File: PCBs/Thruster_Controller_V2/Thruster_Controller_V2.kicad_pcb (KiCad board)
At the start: 4 copper layers, 35.5 x 37 mm, 106 parts, among them J1 PHASE_A, J2 PHASE_B, J3 PHASE_C, J4 Conn_01x01, J5 Pogo Conn, J6 Conn_01x01, J7 Conn_01x01, J8 Conn_01x01, Q1 SIZF906DT, Q2 SIZF906DT, Q3 SIZF906DT, U1 NCP718AMT330, U2 TMS320F280041C, U3 DRV8320S, U8 MCP2562, Y1 20 MHz

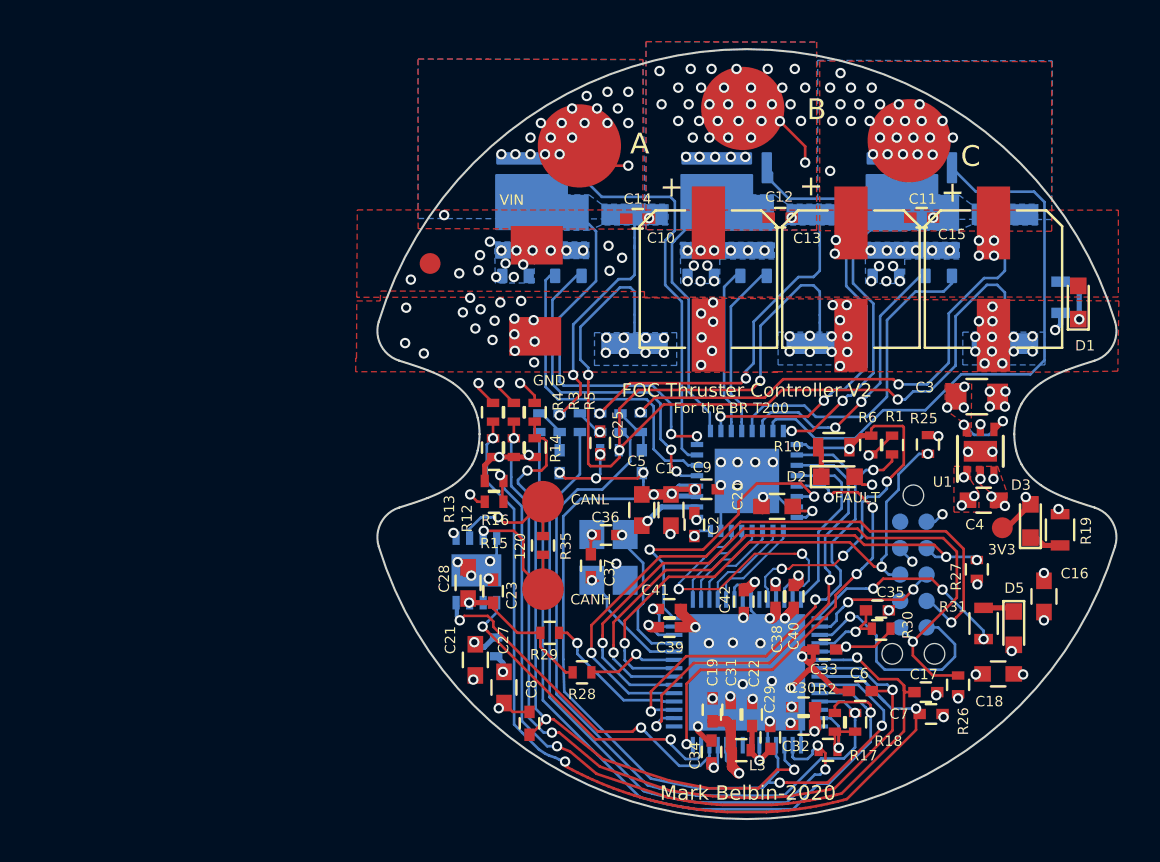
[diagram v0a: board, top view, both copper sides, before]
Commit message: VDD fix
- Fixed VDD error, disconnected it from 3V3 rail.
- Will add any more updates to V2.1 after V2 testing
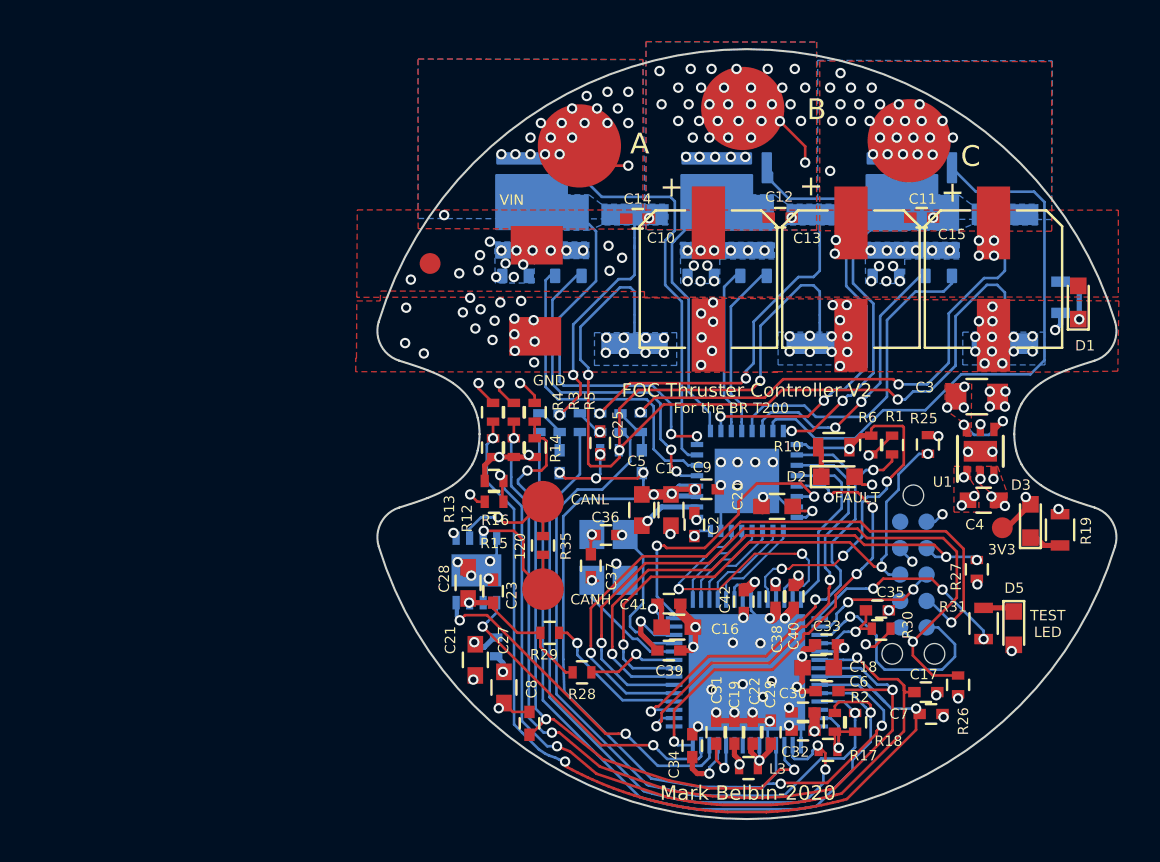
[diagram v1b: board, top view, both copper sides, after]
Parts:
- R19: value 330 -> 180
- moved C16 17.7 mm to (96.7, 107.5), turned to 0 degrees
- moved C18 8.66 mm to (103.4, 109.5), turned to 180 degrees
- moved C6 1.60 mm to (103.8, 110.6)
- moved C19 1.50 mm to (99.4, 112.6)
- moved C39 1.13 mm to (96.2, 108.7)
- moved C31 1.10 mm to (98.5, 112.6)
- moved C34 0.97 mm to (97.4, 113.2)
- moved L3 0.93 mm to (100.1, 114.3)
- moved C22 0.85 mm to (100.3, 112.6)
- moved C32 0.28 mm to (102.7, 112.5)
- moved C33 0.26 mm to (103.8, 108.3)
- moved C29 0.25 mm to (101.2, 112.6)
- moved C41 0.25 mm to (96.2, 106.4)
- moved C30 0.25 mm to (102.7, 111.6)
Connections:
- C16 pad 1: +3V3 -> Net-(C16-Pad1)
- C18 pad 1: +3V3 -> Net-(C18-Pad1)
- C31 pad 1: +3V3 -> Net-(C31-Pad1)
- C33 pad 1: +3V3 -> Net-(C18-Pad1)
- C38 pad 1: +3V3 -> Net-(C38-Pad1)
- C41 pad 1: +3V3 -> Net-(C16-Pad1)
- U2 pad 24: +3V3 -> Net-(C31-Pad1)
- U2 pad 41: +3V3 -> Net-(C16-Pad1)
- U2 pad 5: +3V3 -> Net-(C18-Pad1)
- U2 pad 53: +3V3 -> Net-(C38-Pad1)
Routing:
- net +3V3: track 31.6 -> 18.6 mm, vias 20 -> 16
- net +3.3VA: track 8.61 -> 11.9 mm
- net Net-(C16-Pad1): track 0.00 -> 2.82 mm, vias 0 -> 1
- net Net-(C18-Pad1): track 0.00 -> 2.52 mm, vias 0 -> 1
- net Net-(C31-Pad1): track 0.00 -> 2.46 mm, vias 0 -> 1
- net /Powertrain/VSEN_B: track 41.4 -> 43.1 mm
- net Net-(C38-Pad1): track 0.00 -> 0.92 mm, vias 0 -> 1
- net GND: track 42.5 -> 41.6 mm
- net Net-(C22-Pad1): track 3.39 -> 2.69 mm
- net /TDO: track 34.4 -> 35.0 mm
- net /TCK: track 32.1 -> 32.7 mm
- net /TMS: track 25.8 -> 26.4 mm
- net /TDI: track 26.5 -> 27.0 mm
- net /Powertrain/SPI_CS: track 21.9 -> 22.4 mm
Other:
- board text added: "TEST LED"

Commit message: Layout Changes
- Flipping 3V3 regulator to the bottom of the board for better thermal performance.
- Likewise placing 5V regulator on the bottom. This will require mech changes.
- Need to compress things to the right more
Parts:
- added C43: 1uF, Capacitors_SMD:C_0805, F.Cu at (67.9, 102.6)
- added C44: 1uF, Capacitors_SMD:C_0603, F.Cu at (71.9, 105.2)
- added D4: GREEN, LEDs:LED_0603, F.Cu at (72.1, 102.3)
- added R34: 220, Resistors_SMD:R_0603, F.Cu at (75.9, 102.4)
- added TP2: TestPoint, Thruster_Controller:TestPoint_Pad_D1.0mm, F.Cu at (74.8, 104.6)
- added U4: NCP718BMT500, Housings_DFN_QFN:DFN-6-1EP_2x2mm_Pitch0.65mm, B.Cu at (86.8, 105.4)
- R19: value 180 -> 100
- U8: value MCP2562 -> ATA6561; moved to F.Cu
- moved J4 7.06 mm to (91.0, 108.5)
- moved R29 5.38 mm to (95.1, 110.6), turned to 180 degrees
- moved R35 3.87 mm to (92.0, 107.0), turned to 90 degrees
- moved R28 3.02 mm to (95.1, 109.7), turned to 180 degrees
- moved C28 2.76 mm to (89.4, 105.4)
- moved C23 2.31 mm to (89.6, 107.2), turned to 0 degrees
- moved J6 0.76 mm to (91.0, 105.6)
- moved U8 0.68 mm to (86.8, 105.5)
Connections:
- C23 pad 1: +3V3 -> +5V
- C28 pad 1: +3V3 -> +5V
- U8 pad 3: +3V3 -> +5V
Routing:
- net +3V3: track 18.6 -> 11.4 mm, vias 16 -> 14
- net /CANH: track 6.84 -> 0.00 mm, vias 1 -> 0
- net /CANL: track 6.58 -> 0.00 mm, vias 1 -> 0
- net /TI_MCU/GPIO24: track 7.23 -> 2.76 mm
- net /RXCAN: track 17.2 -> 14.4 mm, vias 2 -> 1
- net /TI_MCU/GPIO32: track 4.37 -> 2.81 mm
- net GND: track 41.6 -> 40.6 mm
- net /Powertrain/PGA_GND: track 44.3 -> 43.5 mm
- net /TXCAN: track 15.2 -> 15.7 mm, vias 2 -> 1
- net +5V: track 0.00 -> 0.18 mm, vias 0 -> 1
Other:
- board text added: "FOC Thruster Controller V2.1"
- board text removed: "FOC Thruster Controller V2"

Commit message: Routing and Layout
- Finished layout
- Finished routing
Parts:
- L1: moved to F.Cu
- U1, U8: moved to B.Cu
- moved TP2 16.7 mm to (91.0, 108.5)
- moved C43 16.7 mm to (84.5, 103.1), turned to 180 degrees
- moved D4 13.6 mm to (85.2, 106.1)
- moved C44 12.7 mm to (84.5, 104.7), turned to 180 degrees
- moved R34 11.6 mm to (86.0, 108.1), turned to 270 degrees
- moved J6 4.00 mm to (91.0, 101.6)
- moved R35 3.95 mm to (90.0, 103.7)
- moved J4 2.92 mm to (91.0, 105.6)
- moved U4 2.92 mm to (84.5, 103.7)
- moved C23 2.68 mm to (88.5, 104.8), turned to 90 degrees
- moved C4 2.40 mm to (111.0, 99.0), turned to 180 degrees
- moved C28 2.05 mm to (87.3, 105.0)
- moved U8 1.46 mm to (87.7, 104.2)
- moved U1 1.24 mm to (111.0, 97.8)
- moved C36 1.14 mm to (94.2, 103.7)
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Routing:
- net +3V3: track 11.4 -> 25.9 mm, vias 14 -> 16
- net GND: track 40.6 -> 49.5 mm, vias 111 -> 112
- net /CANL: track 0.00 -> 6.25 mm, vias 0 -> 1
- net /CANH: track 0.00 -> 5.19 mm, vias 0 -> 1
- net +5V: track 0.18 -> 5.06 mm, vias 1 -> 4
- net /RXCAN: track 14.4 -> 17.7 mm, vias 1 -> 2
- net Net-(D4-Pad1): track 0.00 -> 2.55 mm
- net +BATT: track 11.0 -> 12.9 mm
- net /TI_MCU/GPIO24: track 2.76 -> 4.14 mm
- net /Powertrain/EN_GATE: track 14.2 -> 13.1 mm
- net /Powertrain/VSEN_PVDD: track 41.7 -> 42.6 mm
- net /TXCAN: track 15.7 -> 14.9 mm, vias 1 -> 2
- net /Powertrain/ISEN_C: track 35.6 -> 34.9 mm
- net /Powertrain/ISEN_B: track 32.6 -> 32.0 mm
- net /Powertrain/PGA_GND: track 43.5 -> 42.9 mm
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- added copper zone on B.Cu, net +3V3
- added copper zone on F.Cu, net +5V
- removed copper zone on F.Cu, net +3V3
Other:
- rule trace_min: 0.0889 -> 0

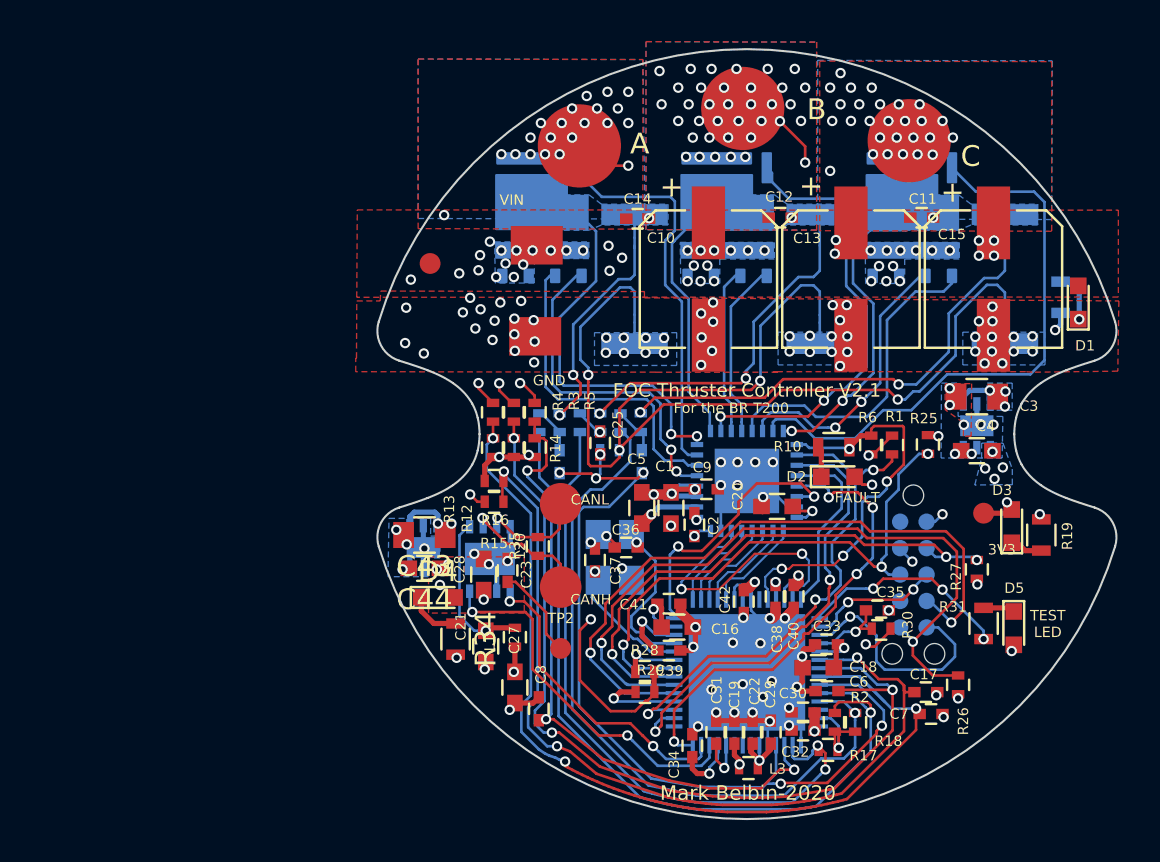
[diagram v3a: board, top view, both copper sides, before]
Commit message: Silk and touchups
- Updated aluminum poly cap, adjusted courtyard
- Fixed silkscreen
- Added more power planes near LDOs
- Cleaned up some routing, still need to have a gooood look before sending this off. But, its 99% ready to go!
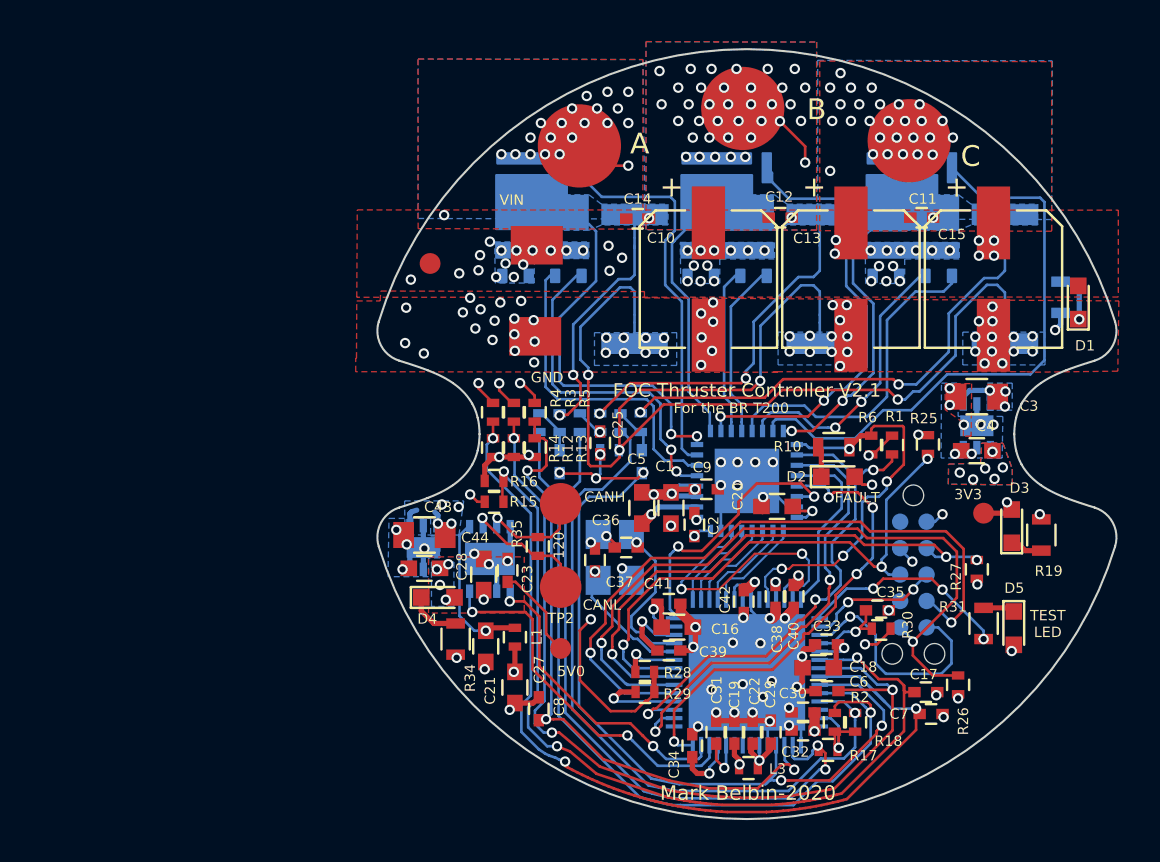
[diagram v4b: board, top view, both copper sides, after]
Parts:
- C10, C13, C15: footprint Capacitors_SMD:CP_Elec_6.3x5.8 -> Thruster_Controller:CP_Elec_6.3x5.8
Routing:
- net +BATT: track 12.9 -> 12.1 mm, vias 56 -> 58
- net +3V3: track 25.9 -> 25.8 mm, vias 16 -> 18
- net +5V: vias 4 -> 5
- added copper zone on F.Cu, net +3V3
- added copper zone on B.Cu, net +5V
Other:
- board text added: "5V0"

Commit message: Updated Footprints
- Moved over to the default KiCAD footprints, the rounded ones.
- Updated all 3D models as well
- Need to fix a bunch of DRC errors ;(
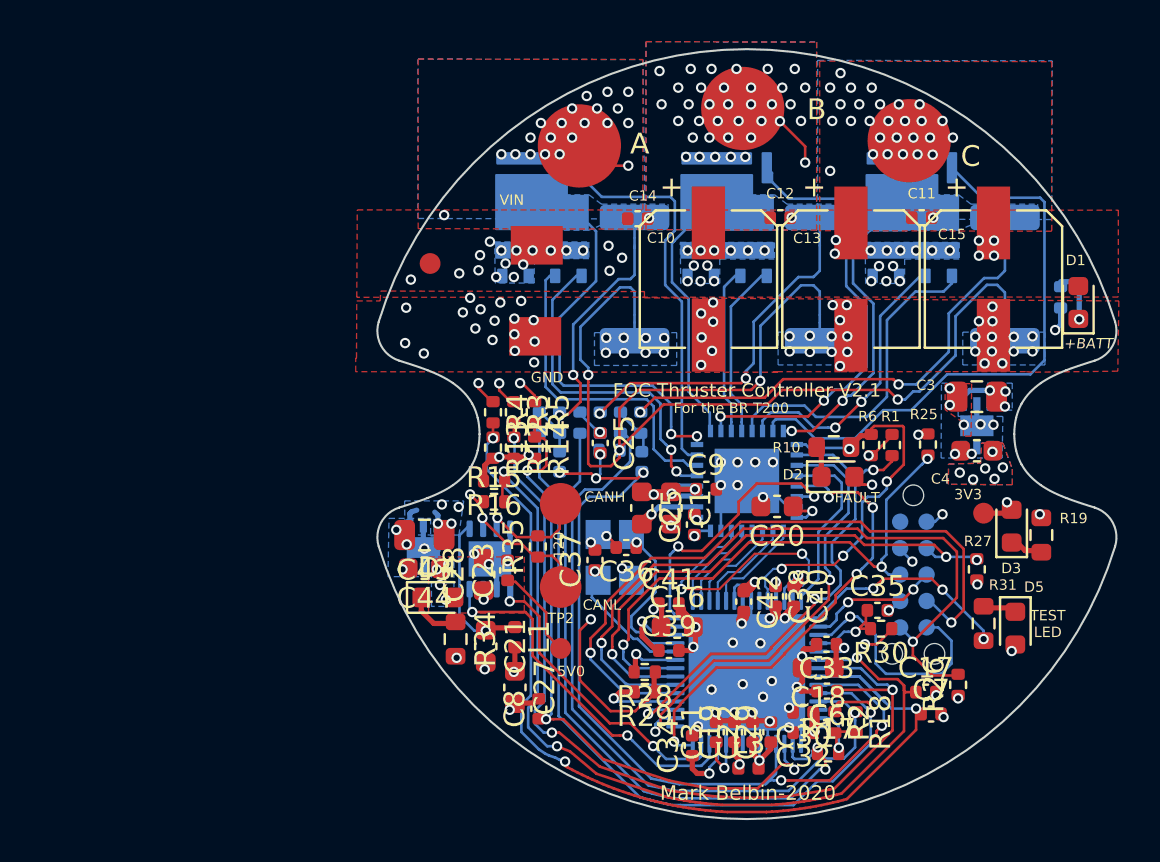
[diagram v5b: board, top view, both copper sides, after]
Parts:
- C1, C16, C18, C20, C21, C27, C28, C4, C44, C5: footprint Capacitors_SMD:C_0603 -> Capacitor_SMD:C_0603_1608Metric
- C11, C12, C14, C17, C19, C2, C22, C23, C24, C25, C26, C29, C30, C31, C32, C33, C34, C35, C36, C37, C38, C39, C40, C41, C42, C6, C7, C8, C9: footprint Capacitors_SMD:C_0402 -> Capacitor_SMD:C_0402_1005Metric
- C3, C43: footprint Capacitors_SMD:C_0805 -> Capacitor_SMD:C_0805_2012Metric
- D1, D2, D3, D4, D5: footprint LEDs:LED_0603 -> LED_SMD:LED_0603_1608Metric
- L1, L3: footprint Inductors_SMD:L_0402 -> Inductor_SMD:L_0402_1005Metric
- R1, R12, R13, R14, R15, R16, R17, R18, R2, R20, R21, R22, R23, R24, R25, R26, R27, R28, R29, R3, R30, R32, R33, R35, R4, R5, R6: footprint Resistors_SMD:R_0402 -> Resistor_SMD:R_0402_1005Metric
- R10, R19, R31, R34: footprint Resistors_SMD:R_0603 -> Resistor_SMD:R_0603_1608Metric
- R11, R8, R9: footprint Resistors_SMD:R_2512 -> Resistor_SMD:R_2512_6332Metric
- R7: footprint Resistors_SMD:R_0603 -> Resistor_SMD:R_0402_1005Metric
- U1, U4: footprint Housings_DFN_QFN:DFN-6-1EP_2x2mm_Pitch0.65mm -> Package_DFN_QFN:DFN-6-1EP_2x2mm_P0.65mm_EP1x1.6mm
- U2: footprint Housings_DFN_QFN:QFN-56-1EP_7x7mm_Pitch0.4mm -> Package_DFN_QFN:QFN-56-1EP_7x7mm_P0.4mm_EP5.6x5.6mm
- U3: footprint Housings_DFN_QFN:WQFN-32-1EP_5x5mm_Pitch0.5mm -> Package_DFN_QFN:WQFN-32-1EP_5x5mm_P0.5mm_EP3.1x3.1mm
- U8: footprint Housings_DFN_QFN:DFN-8-1EP_3x3mm_Pitch0.65mm -> Package_DFN_QFN:DFN-8-1EP_3x3mm_P0.65mm_EP1.7x2.05mm
- moved R17 0.17 mm to (103.9, 113.6)
- moved C32 0.10 mm to (102.7, 112.6)
- moved D5 0.08 mm to (112.9, 107.6)
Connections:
- J5 pad 10: /TRST -> (no net)
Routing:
- net Net-(C22-Pad1): track 2.69 -> 3.61 mm
- net /Powertrain/DAC: track 4.85 -> 3.93 mm
- net GND: track 49.5 -> 50.2 mm
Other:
- rule pad_to_mask_clearance: 0.051 -> 0
- rule trace_min: 0 -> 0.1
- board text added: "+BATT"

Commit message: DRC
- Fixed all new DRC errors created by new footprints.
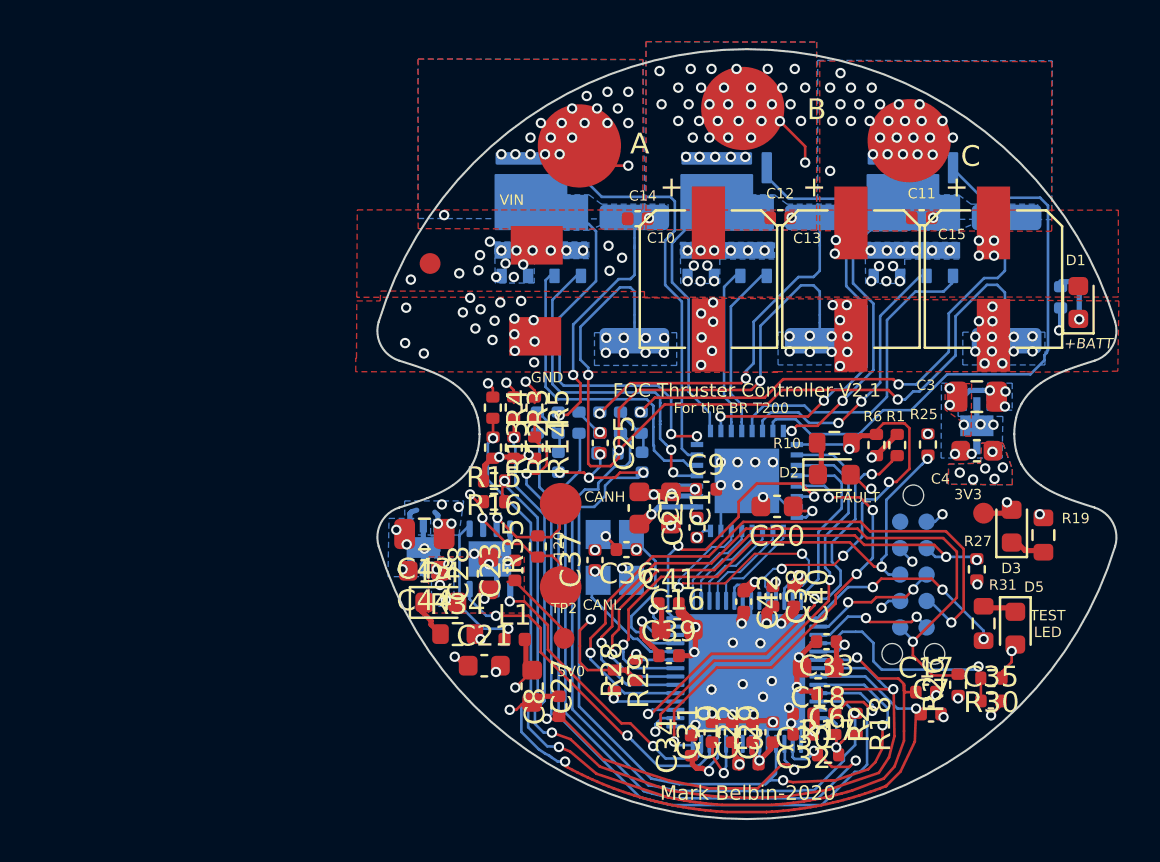
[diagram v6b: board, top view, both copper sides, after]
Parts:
- moved C35 6.98 mm to (111.7, 111.1)
- moved R30 5.81 mm to (111.8, 110.0)
- moved R29 1.57 mm to (93.6, 110.1), turned to 270 degrees
- moved C8 0.98 mm to (91.0, 111.3)
- moved C21 0.93 mm to (87.4, 109.4), turned to 0 degrees
- moved C27 0.83 mm to (89.7, 110.4)
- moved TP2 0.51 mm to (91.2, 108.1)
- moved R28 0.43 mm to (94.7, 109.6), turned to 90 degrees
- moved C23 0.35 mm to (88.8, 104.8)
- moved D4 0.28 mm to (85.3, 106.3)
- moved R34 0.26 mm to (86.1, 107.9), turned to 0 degrees
- moved C39 0.25 mm to (96.2, 108.9)
- moved R1 0.25 mm to (107.2, 98.8)
- moved R6 0.25 mm to (106.2, 98.8)
- moved C28 0.23 mm to (87.6, 105.0)
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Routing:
- net /TI_MCU/~RESET~: track 4.02 -> 10.9 mm
- net GND: track 50.2 -> 55.8 mm, vias 112 -> 113
- net /SCI_RX: track 11.4 -> 5.94 mm, vias 1 -> 2
- net /Powertrain/VSEN_A: track 47.6 -> 44.4 mm
- net /Powertrain/ISEN_B: track 31.9 -> 34.1 mm
- net /Powertrain/PGA_GND: track 42.7 -> 44.2 mm
- net +3.3VA: track 12.2 -> 13.5 mm
- net Net-(C18-Pad1): track 2.52 -> 3.77 mm
- net +3V3: track 25.8 -> 24.9 mm
- net /TI_MCU/GPIO24: track 4.14 -> 3.31 mm
- net /TI_MCU/GPIO32: track 2.81 -> 1.99 mm
- net /RXCAN: track 17.3 -> 16.6 mm
- net Net-(C31-Pad1): track 2.46 -> 3.11 mm
- net /Powertrain/VSEN_C: track 31.4 -> 30.8 mm
- net /Powertrain/VSEN_B: track 43.4 -> 43.9 mm
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
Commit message: V2.1
- Fixed silk
- Cleaned up routing
- Exported Gerbers
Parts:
- moved R26 0.97 mm to (110.2, 111.3)
- moved C7 0.28 mm to (108.6, 111.9)
- moved C17 0.16 mm to (108.6, 110.8)
- moved R15 0.13 mm to (87.7, 101.5)
- moved R30 0.07 mm to (111.7, 110.0)
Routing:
- net /TDO: track 34.7 -> 35.4 mm
- net /TI_MCU/~RESET~: track 10.9 -> 10.3 mm
